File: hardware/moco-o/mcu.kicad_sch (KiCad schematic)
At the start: 14 parts, among them U3 8MHz, U4 STM32F405RGTx

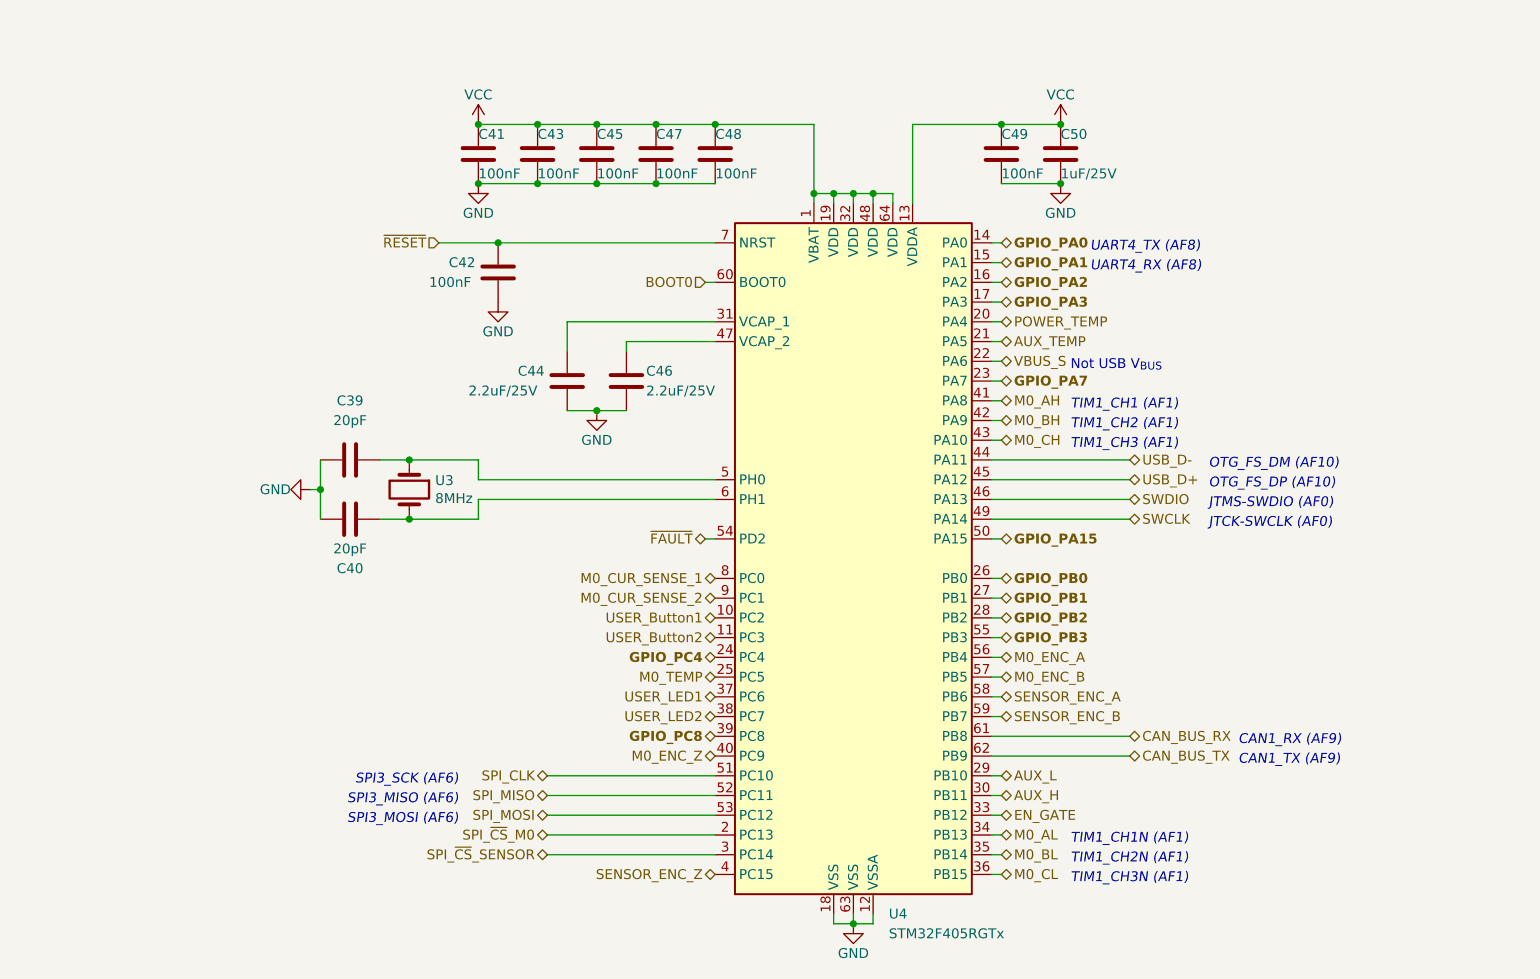
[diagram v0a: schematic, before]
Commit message: Change to DRV8323H
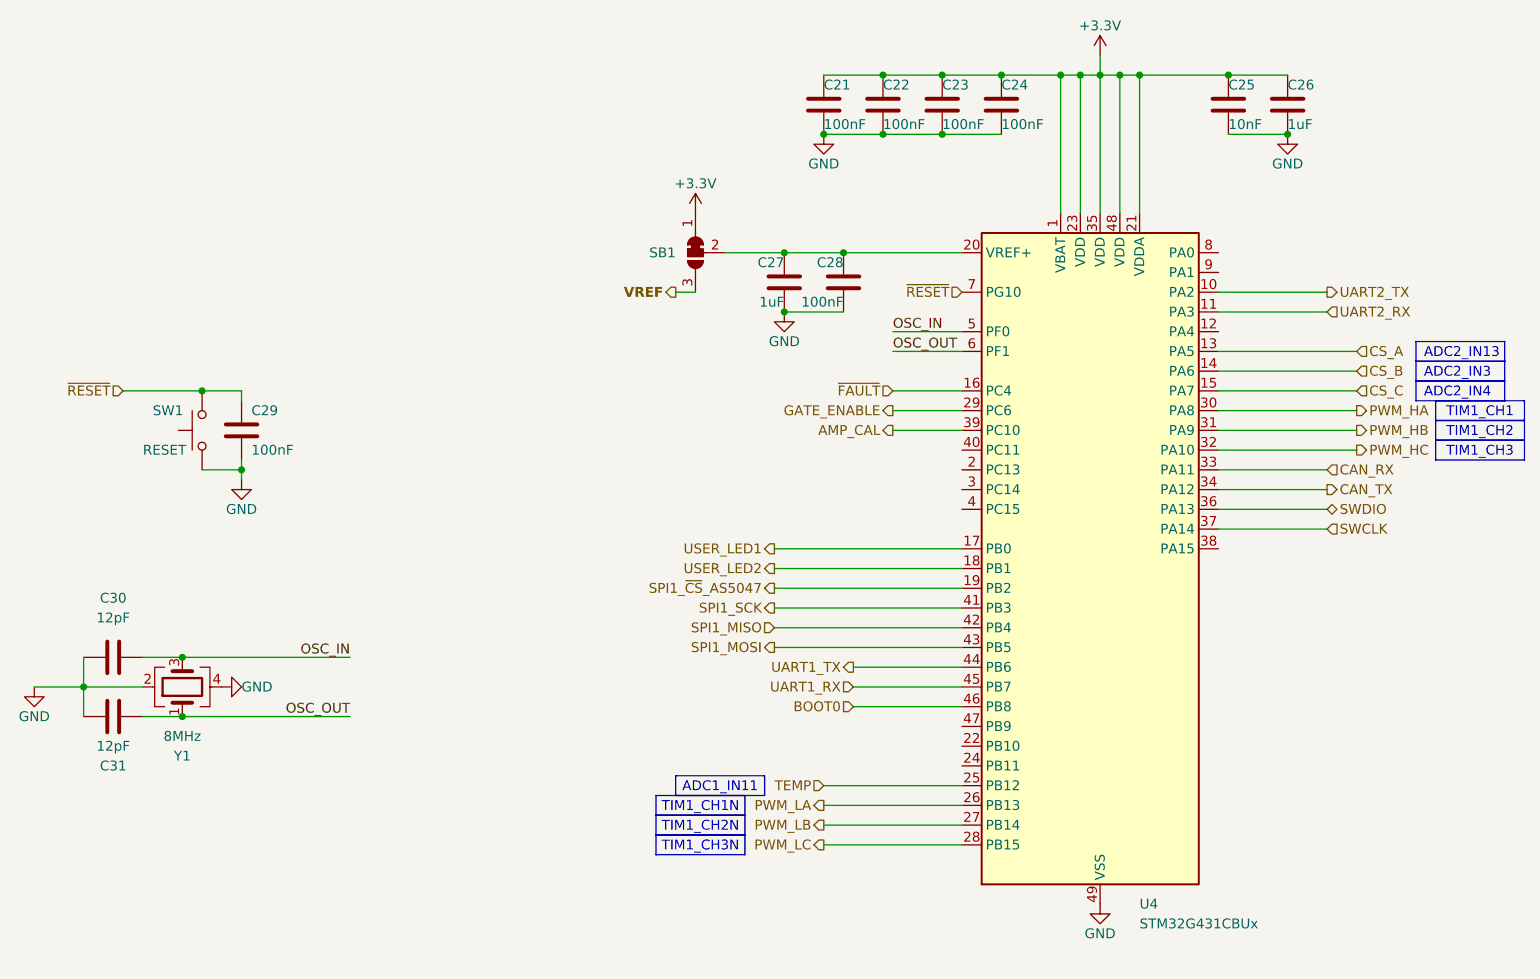
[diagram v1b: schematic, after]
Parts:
- removed C39, C40: 20pF, Capacitor_SMD:C_0402_1005Metric, symbol Device:C
- removed C41, C42, C43, C45, C47, C48, C49: 100nF, Capacitor_SMD:C_0402_1005Metric, symbol Device:C
- removed C44, C46: 2.2uF/25V, Capacitor_SMD:C_0402_1005Metric, symbol Device:C
- removed C50: 1uF/25V, Capacitor_SMD:C_0402_1005Metric, symbol Device:C
- removed U3: 8MHz, Crystal:Crystal_SMD_5032-2Pin_5.0x3.2mm, symbol Device:Crystal
- removed U4: STM32F405RGTx, Package_QFP:LQFP-64_10x10mm_P0.5mm, symbol MCU_ST_STM32F4:STM32F405RGTx
- added C21, C22, C23, C24, C28, C29: 100nF, Capacitor_SMD:C_0402_1005Metric, symbol Device:C
- added C25: 10nF, Capacitor_SMD:C_0402_1005Metric, symbol Device:C
- added C26, C27: 1uF, Capacitor_SMD:C_0402_1005Metric, symbol Device:C
- added C30, C31: 12pF, Capacitor_SMD:C_0402_1005Metric, symbol Device:C
- added SB1: SolderJumper_3_Bridged12, Jumper:SolderJumper-3_P1.3mm_Bridged12_RoundedPad1.0x1.5mm, symbol Jumper:SolderJumper_3_Bridged12
- added SW1: RESET, Button_Switch_SMD:SW_SPST_TL3342, symbol Switch:SW_Push
- added U4: STM32G431CBUx, Package_DFN_QFN:QFN-48-1EP_7x7mm_P0.5mm_EP5.6x5.6mm, symbol MCU_ST_STM32G4:STM32G431CBUx
- added Y1: 8MHz, Crystal:Crystal_SMD_3225-4Pin_3.2x2.5mm, symbol Device:Crystal_GND24
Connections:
- net BOOT0: now also U4.46 (PB8)
- net GND: now also C21.2, C22.2, C23.2, C24.2, C25.2, C26.2, C27.2, C28.2, C29.2, C30.1, C31.1, SW1.1, U4.49 (VSS), Y1.2, Y1.4
- net SWCLK: now also U4.37 (PA14)
- net SWDIO: now also U4.36 (PA13)
- net USER_LED1: now also U4.17 (PB0)
- net USER_LED2: now also U4.18 (PB1)
- net ~{FAULT}: now also U4.16 (PC4)
- net ~{RESET}: now also C29.1, SW1.2, U4.7 (PG10)
- new net: C27.1, C28.1, SB1.2 (C), U4.20 (VREF+)
- new net +3.3V: C21.1, C22.1, C23.1, C24.1, C25.1, C26.1, SB1.1 (A), U4.1 (VBAT), U4.21 (VDDA), U4.23 (VDD), U4.35 (VDD), U4.48 (VDD)
- new net AMP_CAL: U4.39 (PC10)
- new net CAN_RX: U4.33 (PA11)
- new net CAN_TX: U4.34 (PA12)
- new net CS_A: U4.13 (PA5)
- new net CS_B: U4.14 (PA6)
- new net CS_C: U4.15 (PA7)
- new net GATE_ENABLE: U4.29 (PC6)
- new net OSC_IN: C30.2, U4.5 (PF0), Y1.3
- new net OSC_OUT: C31.2, U4.6 (PF1), Y1.1
- new net PWM_HA: U4.30 (PA8)
- new net PWM_HB: U4.31 (PA9)
- new net PWM_HC: U4.32 (PA10)
- new net PWM_LA: U4.26 (PB13)
- new net PWM_LB: U4.27 (PB14)
- new net PWM_LC: U4.28 (PB15)
- new net SPI1_MISO: U4.42 (PB4)
- new net SPI1_MOSI: U4.43 (PB5)
- new net SPI1_SCK: U4.41 (PB3)
- new net SPI1_~{CS}_AS5047: U4.19 (PB2)
- new net TEMP: U4.25 (PB12)
- new net UART1_RX: U4.45 (PB7)
- new net UART1_TX: U4.44 (PB6)
- new net UART2_RX: U4.11 (PA3)
- new net UART2_TX: U4.10 (PA2)
- new net VREF: SB1.3 (B)
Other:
- note removed: "CAN1_RX (AF9)"
- note removed: "CAN1_TX (AF9)"
- note removed: "JTCK-SWCLK (AF0)"
- note removed: "JTMS-SWDIO (AF0)"
- note removed: "Not USB V_{BUS}"
- note removed: "OTG_FS_DM (AF10)"
- note removed: "OTG_FS_DP (AF10)"
- note removed: "SPI3_MISO (AF6)"
- note removed: "SPI3_MOSI (AF6)"
- note removed: "SPI3_SCK (AF6)"
- note removed: "TIM1_CH1 (AF1)"
- note removed: "TIM1_CH1N (AF1)"
- note removed: "TIM1_CH2 (AF1)"
- note removed: "TIM1_CH2N (AF1)"
- note removed: "TIM1_CH3 (AF1)"
- note removed: "TIM1_CH3N (AF1)"
- note removed: "UART4_RX (AF8)"
- note removed: "UART4_TX (AF8)"
